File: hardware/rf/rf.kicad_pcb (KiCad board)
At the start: 4 copper layers, 31.8 x 25.4 mm, 51 parts, among them J1 BGT24_Module_Castellations, J2 SMP, J3 SMP, J4 SMP, U1 ECS-2520S33-400, U2 LMX2491, U3 VQFN-32-9

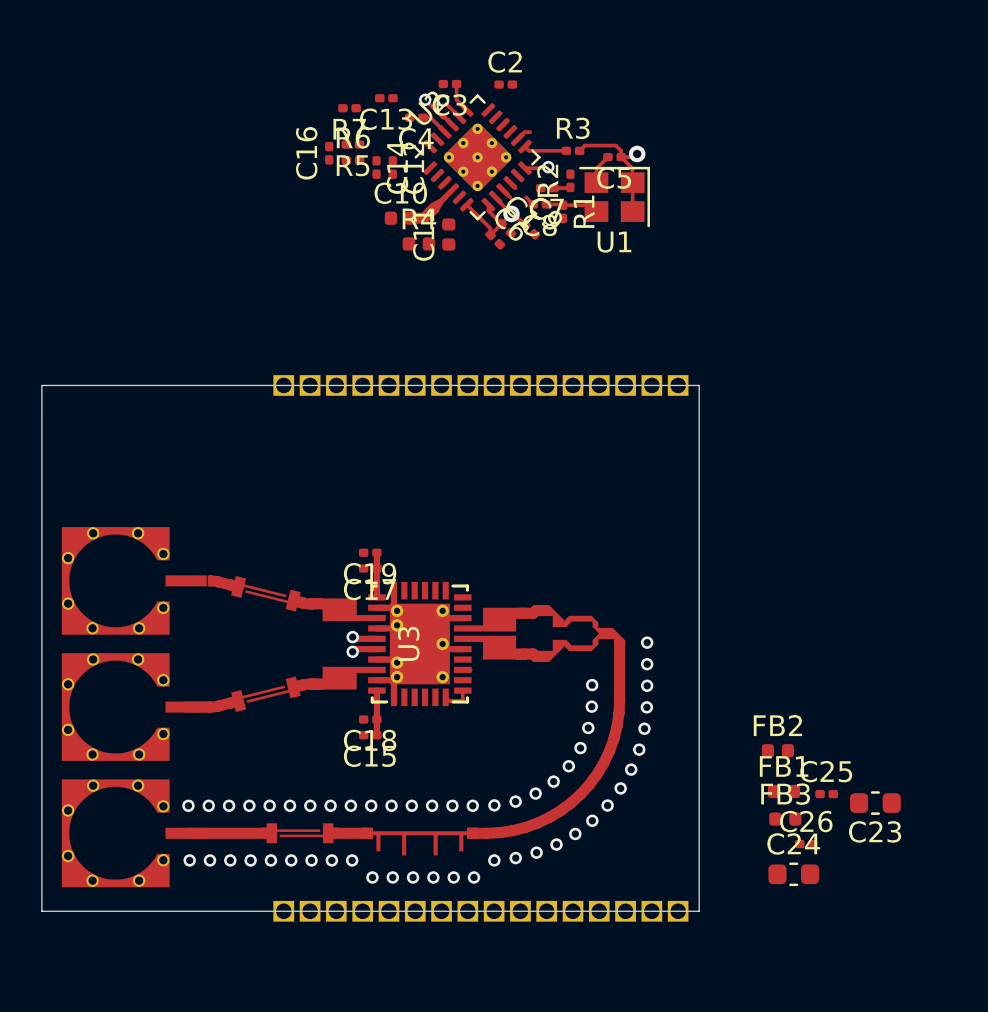
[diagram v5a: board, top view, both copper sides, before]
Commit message: BGT24 module layout of PLL and via stitching
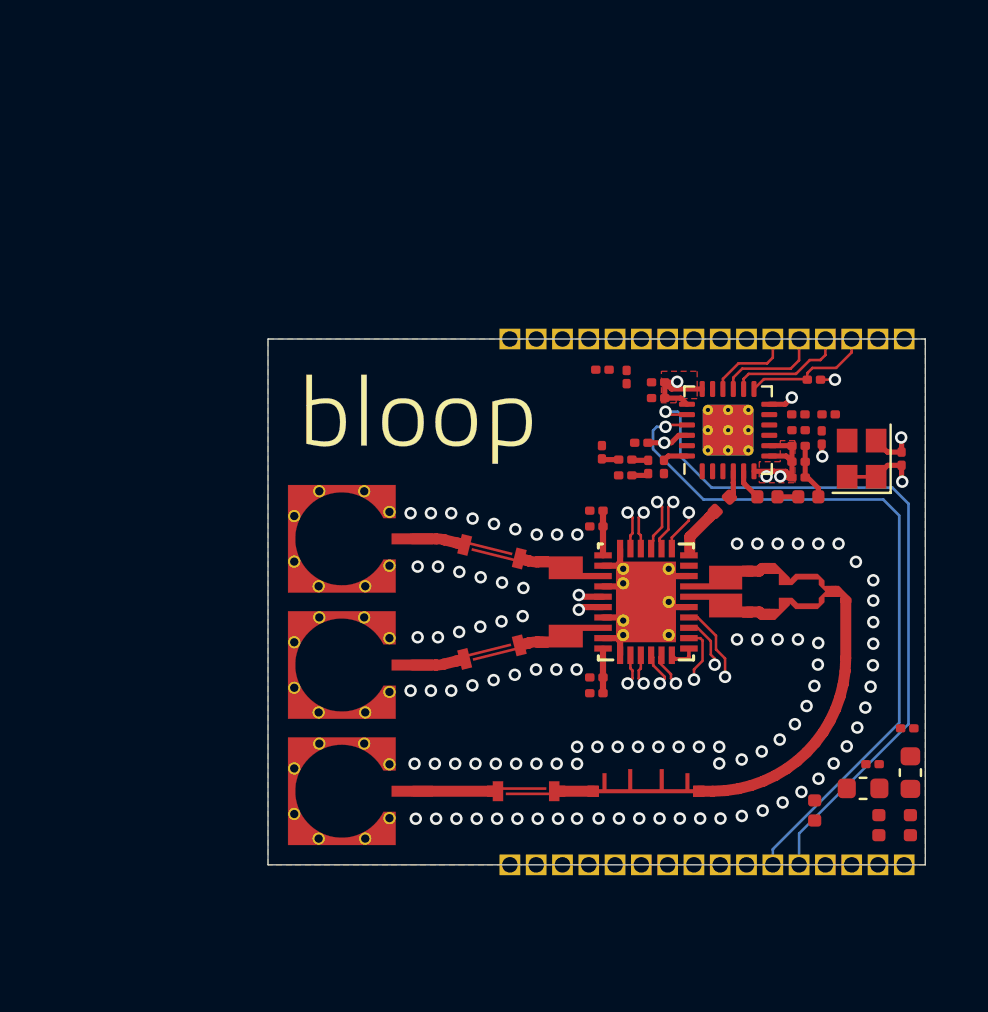
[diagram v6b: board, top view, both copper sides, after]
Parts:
- removed the ? at (132.6, 100.0)
- removed the ? at (137.5, 98.9)
- removed the ? at (133.0, 93.9)
- removed the ? at (137.0, 95.0)
- removed the ? at (143.9, 75.4)
- added ?: , , F.Cu at (143.5, 98.0)
- added ?: , , F.Cu at (148.4, 96.8)
- added ?: , , F.Cu at (143.9, 91.9)
- added ?: , , F.Cu at (148.0, 92.9)
- added ~: LOGO, bloop:bloop_logo_text_silkandcopper, F.Cu at (142.7, 86.2)
- U3: value VQFN-32-9 -> BGT24MTR12
- moved R4 22.4 mm to (161.5, 89.8), turned to 180 degrees
- moved C10 20.8 mm to (157.3, 90.2), turned to 45 degrees
- moved R5 20.7 mm to (152.6, 88.8)
- moved C5 20.1 mm to (166.0, 88.0), turned to 90 degrees
- moved C11 19.9 mm to (159.5, 89.8), turned to 180 degrees
- moved C16 19.5 mm to (151.5, 87.7)
- moved R6 19.5 mm to (152.6, 88.0)
- moved C14 19.5 mm to (153.7, 88.4)
- moved C12 19.5 mm to (154.5, 88.4)
- moved C4 19.1 mm to (153.4, 87.2)
- moved R7 18.6 mm to (152.7, 84.0), turned to 270 degrees
- moved C6 18.6 mm to (161.0, 88.9), turned to 0 degrees
- moved C1 18.1 mm to (161.0, 88.1), turned to 0 degrees
- moved U2 17.9 mm to (157.6, 86.6), turned to 90 degrees
- moved C3 17.6 mm to (154.2, 84.3)
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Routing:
- net /PLL_TRIG1: track 1.12 -> 35.5 mm
- net /PLL_TRIG2: track 1.80 -> 35.3 mm
- net /SPI_MOSI: track 0.00 -> 29.4 mm, vias 0 -> 1
- net /PLL_MOD: track 1.15 -> 30.0 mm
- net /SPI_CLK: track 1.13 -> 27.2 mm, vias 0 -> 1
- net /IF2_Q-: track 0.00 -> 13.7 mm, vias 0 -> 1
- net /IF2_Q+: track 0.00 -> 13.7 mm, vias 0 -> 1
- net /IF1_Q+: track 0.00 -> 13.4 mm, vias 0 -> 1
- net /IF1_Q-: track 0.00 -> 13.2 mm, vias 0 -> 1
- net /~SPI_BGT24_CS: track 0.00 -> 12.4 mm, vias 0 -> 1
- net /IF2_I-: track 0.00 -> 11.9 mm, vias 0 -> 1
- net /IF2_I+: track 0.00 -> 11.9 mm, vias 0 -> 1
- net /IF1_I+: track 0.00 -> 11.5 mm, vias 0 -> 1
- net /IF1_I-: track 0.00 -> 11.5 mm, vias 0 -> 1
- net /PLL_DIV_MCU: track 0.00 -> 11.1 mm, vias 0 -> 1
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- added copper zone on F.Cu, net +3V3_PLL
- added copper zone on F.Cu, net GNDRF
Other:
- net class Differential_IQ added: clearance 0.127, trace_width 0.127, via_dia 0.8, via_drill 0.4

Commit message: BGT24 module final draft layout. Ready for review
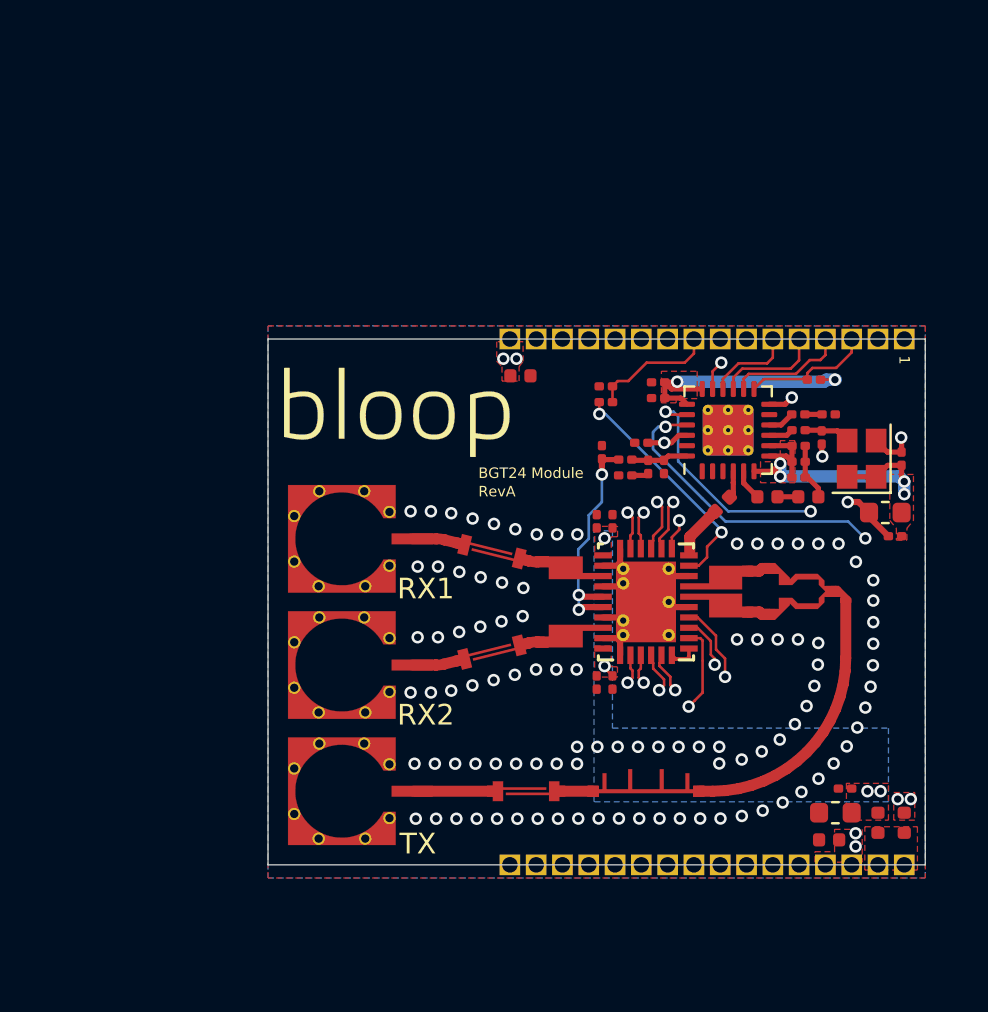
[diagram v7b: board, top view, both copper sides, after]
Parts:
- added FB2: Ferrite_Bead, Inductor_SMD:L_0402_1005Metric, F.Cu at (147.6, 84.0)
- moved C23 12.6 mm to (165.2, 90.6), turned to 180 degrees
- moved C25 9.30 mm to (165.7, 91.7), turned to 180 degrees
- moved C24 1.78 mm to (162.8, 105.1)
- moved C26 1.78 mm to (163.3, 103.9)
- moved FB1 1.58 mm to (162.5, 106.4), turned to 180 degrees
- moved R7 1.57 mm to (151.7, 85.3), turned to 180 degrees
- moved ~ 1.13 mm to (141.6, 85.9)
- moved C19 0.93 mm to (152.0, 91.0), turned to 90 degrees
- moved C15 0.93 mm to (152.0, 98.8), turned to 270 degrees
- moved C13 0.82 mm to (151.7, 84.5)
- moved FB3 0.32 mm to (166.1, 105.6)
- moved C17 0.25 mm to (151.3, 91.0), turned to 90 degrees
- moved C18 0.25 mm to (151.3, 98.8), turned to 270 degrees
- moved FB4 0.12 mm to (164.8, 105.6)
- renumbered FB2 to FB3, FB3 to FB4
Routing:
- net +3V3_PLL: track 17.7 -> 58.7 mm, vias 7 -> 9
- net /PLL_MUX: track 0.00 -> 26.7 mm, vias 0 -> 1
- net Net-(R7-Pad2): track 0.00 -> 11.4 mm, vias 0 -> 2
- net Net-(C16-Pad1): track 3.25 -> 11.0 mm, vias 2 -> 3
- net /BGT24_ANA: track 0.00 -> 6.05 mm
- net +3V3_RF: track 4.32 -> 0.64 mm, vias 0 -> 4
- net GND: track 2.80 -> 5.57 mm, vias 2 -> 7
- net /40MHZ_CLK_OUT: track 0.44 -> 2.67 mm
- net /PLL_TRIG1: track 35.5 -> 33.4 mm, vias 1 -> 2
- net /PLL_TRIG2: track 35.3 -> 33.3 mm, vias 1 -> 2
- net /IF2_I-: track 11.9 -> 13.4 mm
- net /IF2_I+: track 11.9 -> 13.4 mm
- net Net-(C7-Pad2): track 0.00 -> 1.30 mm
- net Net-(C8-Pad2): track 0.00 -> 1.20 mm
- net /IF2_Q+: track 13.7 -> 14.7 mm
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- added copper zone on B.Cu, net +3V3_RF
- added copper zone on F.Cu, net +3V3_RF
- added copper zone on B.Cu, net GND
- added copper zone on F.Cu, net GND
- added copper zone on In1.Cu, net GNDRF
- added copper zone on F.Cu, net PWR_IN
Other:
- net class Differential_IQ removed
- board text added: "1"
- board text added: "BGT24 Module"
- board text added: "RX1"
- board text added: "RX2"
- board text added: "RevA"
- board text added: "TX"

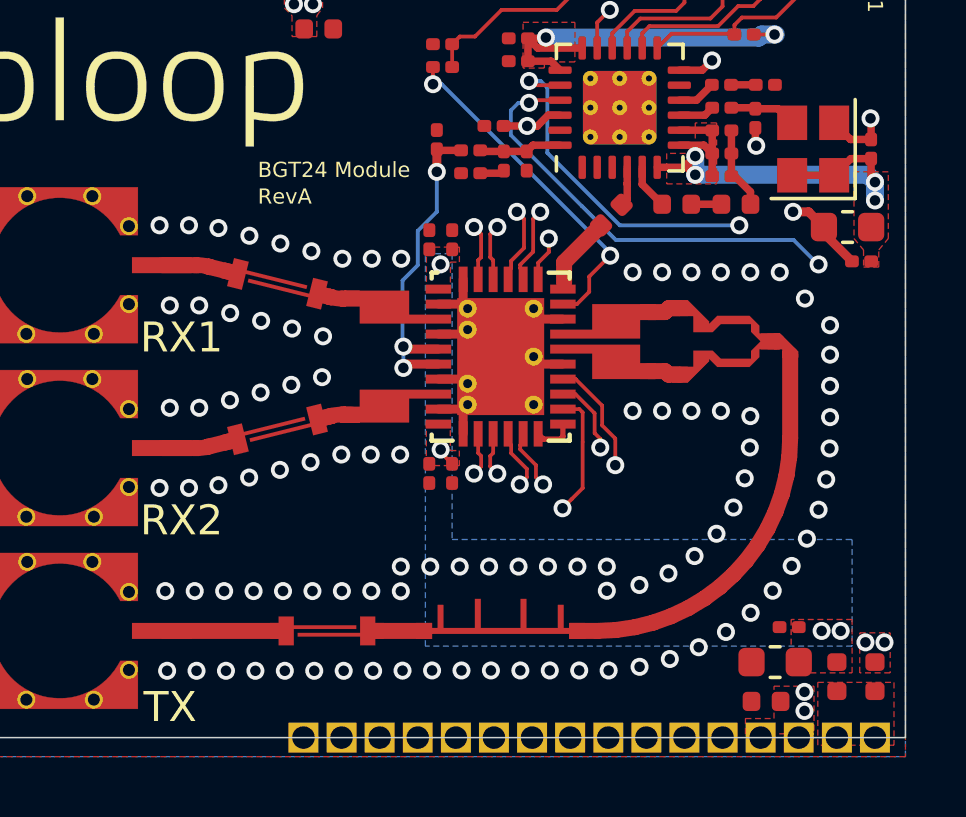
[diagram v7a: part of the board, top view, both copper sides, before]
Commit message: Generated schematic pdf and FAB files for review of revA  BGT24 Module
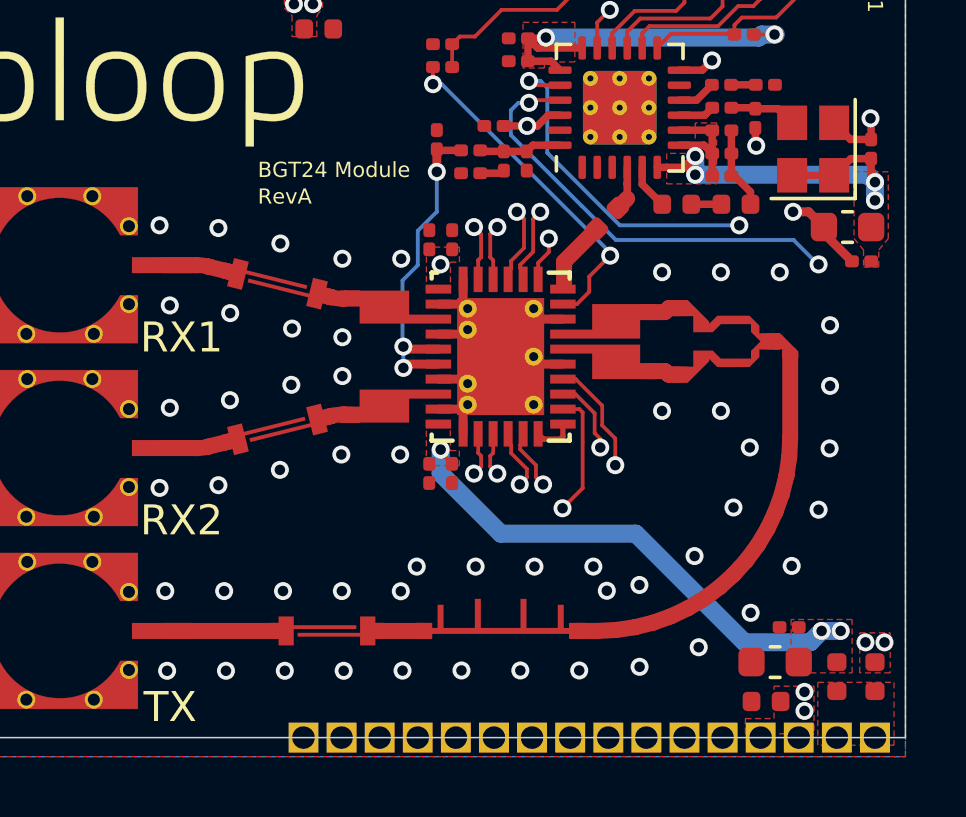
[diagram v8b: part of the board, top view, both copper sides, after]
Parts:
- moved C10 0.16 mm to (157.2, 90.3)
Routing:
- net +3V3_RF: track 0.64 -> 23.4 mm
- net /IF2_I-: track 13.4 -> 11.6 mm
- net /IF2_I+: track 13.4 -> 11.6 mm
- net /IF2_Q+: track 14.7 -> 14.1 mm
- net /IF2_Q-: track 14.6 -> 14.1 mm
- net GNDRF: track 13.2 -> 13.7 mm, vias 98 -> 53
- removed copper zone on B.Cu, net +3V3_RF
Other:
- rule pad_to_mask_clearance: 0.051 -> 0.03
- rule solder_mask_min_width: 0.25 -> 0.07
